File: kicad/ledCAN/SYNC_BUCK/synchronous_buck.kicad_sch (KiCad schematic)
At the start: 22 parts

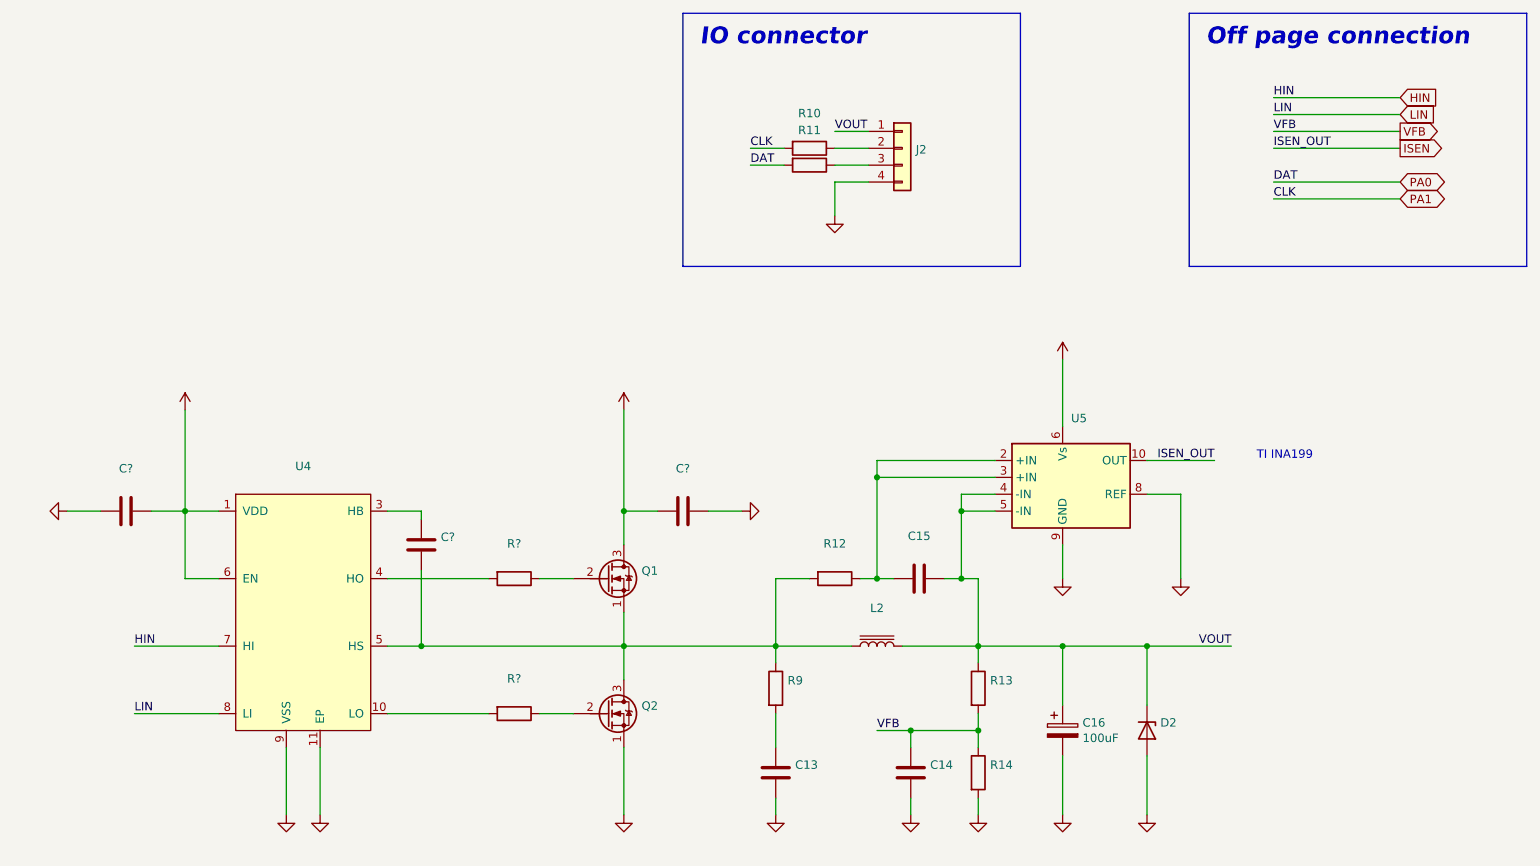
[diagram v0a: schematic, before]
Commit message: Update page settings
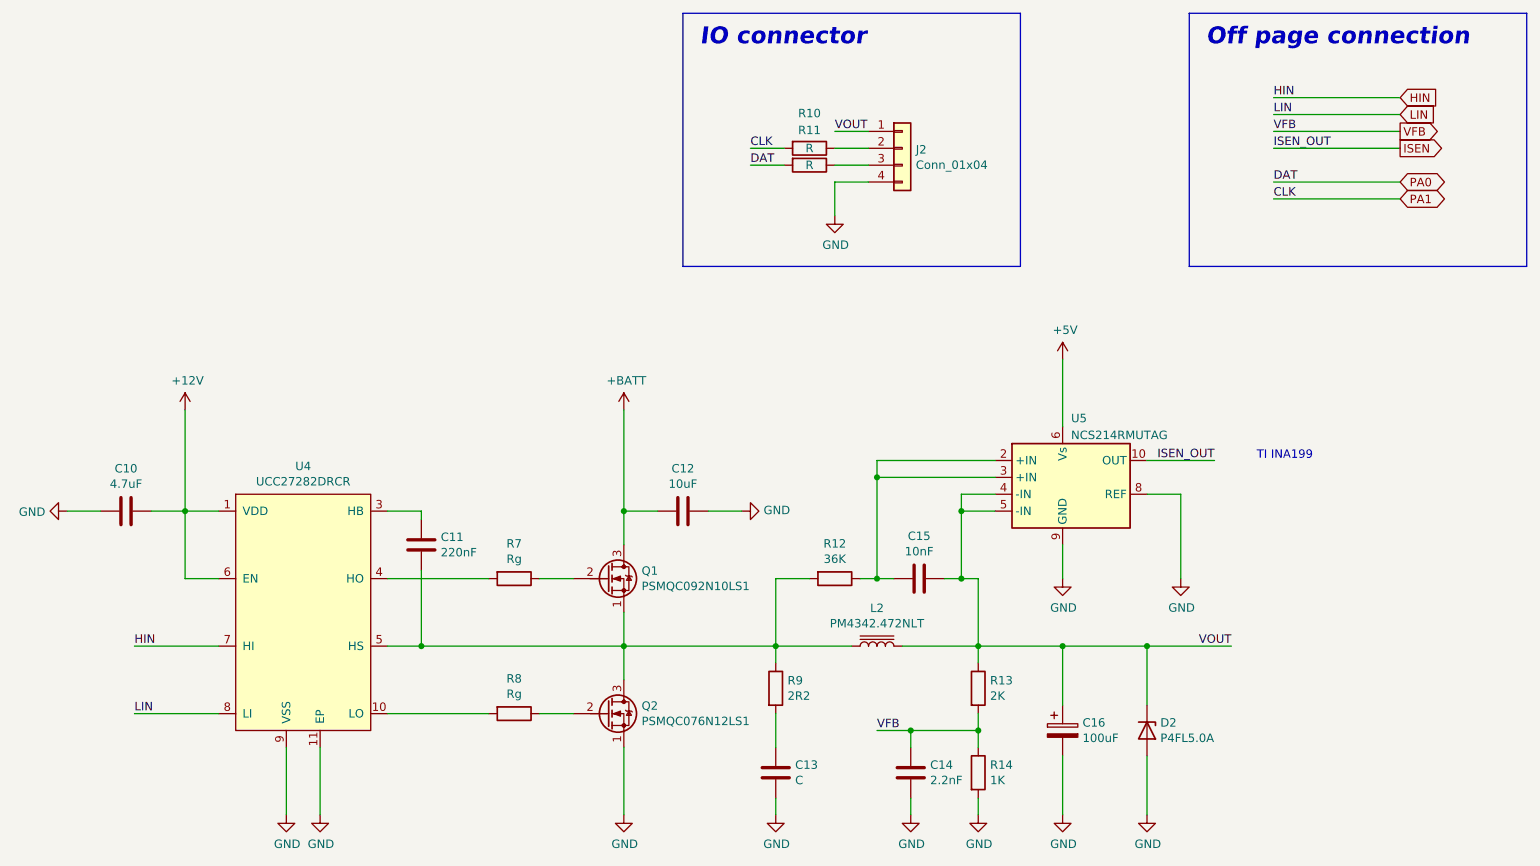
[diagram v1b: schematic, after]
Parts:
- C10: renamed from C?; value (none) -> 4.7uF; footprint (none) -> Capacitor_SMD:C_0603_1608Metric
- C11: renamed from C?; value (none) -> 220nF; footprint (none) -> Capacitor_SMD:C_0603_1608Metric
- C12: renamed from C?; value (none) -> 10uF; footprint (none) -> Capacitor_SMD:C_1210_3225Metric
- C13: value (none) -> C; footprint (none) -> Capacitor_SMD:C_0805_2012Metric_Pad1.18x1.45mm_HandSolder
- C14: value (none) -> 2.2nF; footprint (none) -> Capacitor_SMD:C_0603_1608Metric
- C15: value (none) -> 10nF; footprint (none) -> Capacitor_SMD:C_0603_1608Metric
- D2: value (none) -> P4FL5.0A; footprint (none) -> Diode_SMD:D_SOD-123F
- J2: value (none) -> Conn_01x04; footprint (none) -> IO_CONN:IO_CONN
- L2: value (none) -> PM4342.472NLT; footprint (none) -> Bourns_SRP1038AA:INDPM110100X400N
- Q1: value (none) -> PSMQC092N10LS1; footprint (none) -> PANJIT_DFN:PANJIT_DFN5060-8L
- Q2: value (none) -> PSMQC076N12LS1; footprint (none) -> PANJIT_DFN:PANJIT_DFN5060-8L
- R10, R11: value (none) -> R; footprint (none) -> Resistor_SMD:R_0603_1608Metric
- R12: value (none) -> 36K; footprint (none) -> Resistor_SMD:R_0603_1608Metric
- R13: value (none) -> 2K; footprint (none) -> Resistor_SMD:R_0603_1608Metric
- R14: value (none) -> 1K; footprint (none) -> Resistor_SMD:R_0603_1608Metric
- R7, R8: renamed from R?; value (none) -> Rg; footprint (none) -> Resistor_SMD:R_0603_1608Metric
- R9: value (none) -> 2R2; footprint (none) -> Resistor_SMD:R_0805_2012Metric
- U4: value (none) -> UCC27282DRCR; footprint (none) -> Package_SON:Texas_DRC0010J_ThermalVias
- U5: value (none) -> NCS214RMUTAG; footprint (none) -> Package_DFN_QFN:UQFN-10_1.4x1.8mm_P0.4mm
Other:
- company: DANCHOUZHOU -> City Science Lab @ Taipei Tech /a cooperation with the MIT Media Lab
